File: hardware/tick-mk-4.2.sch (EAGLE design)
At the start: 28 parts, among them IC1 ATMEGA328P, IC2 DS1338, IC3 LM1117, Y1 16MHz

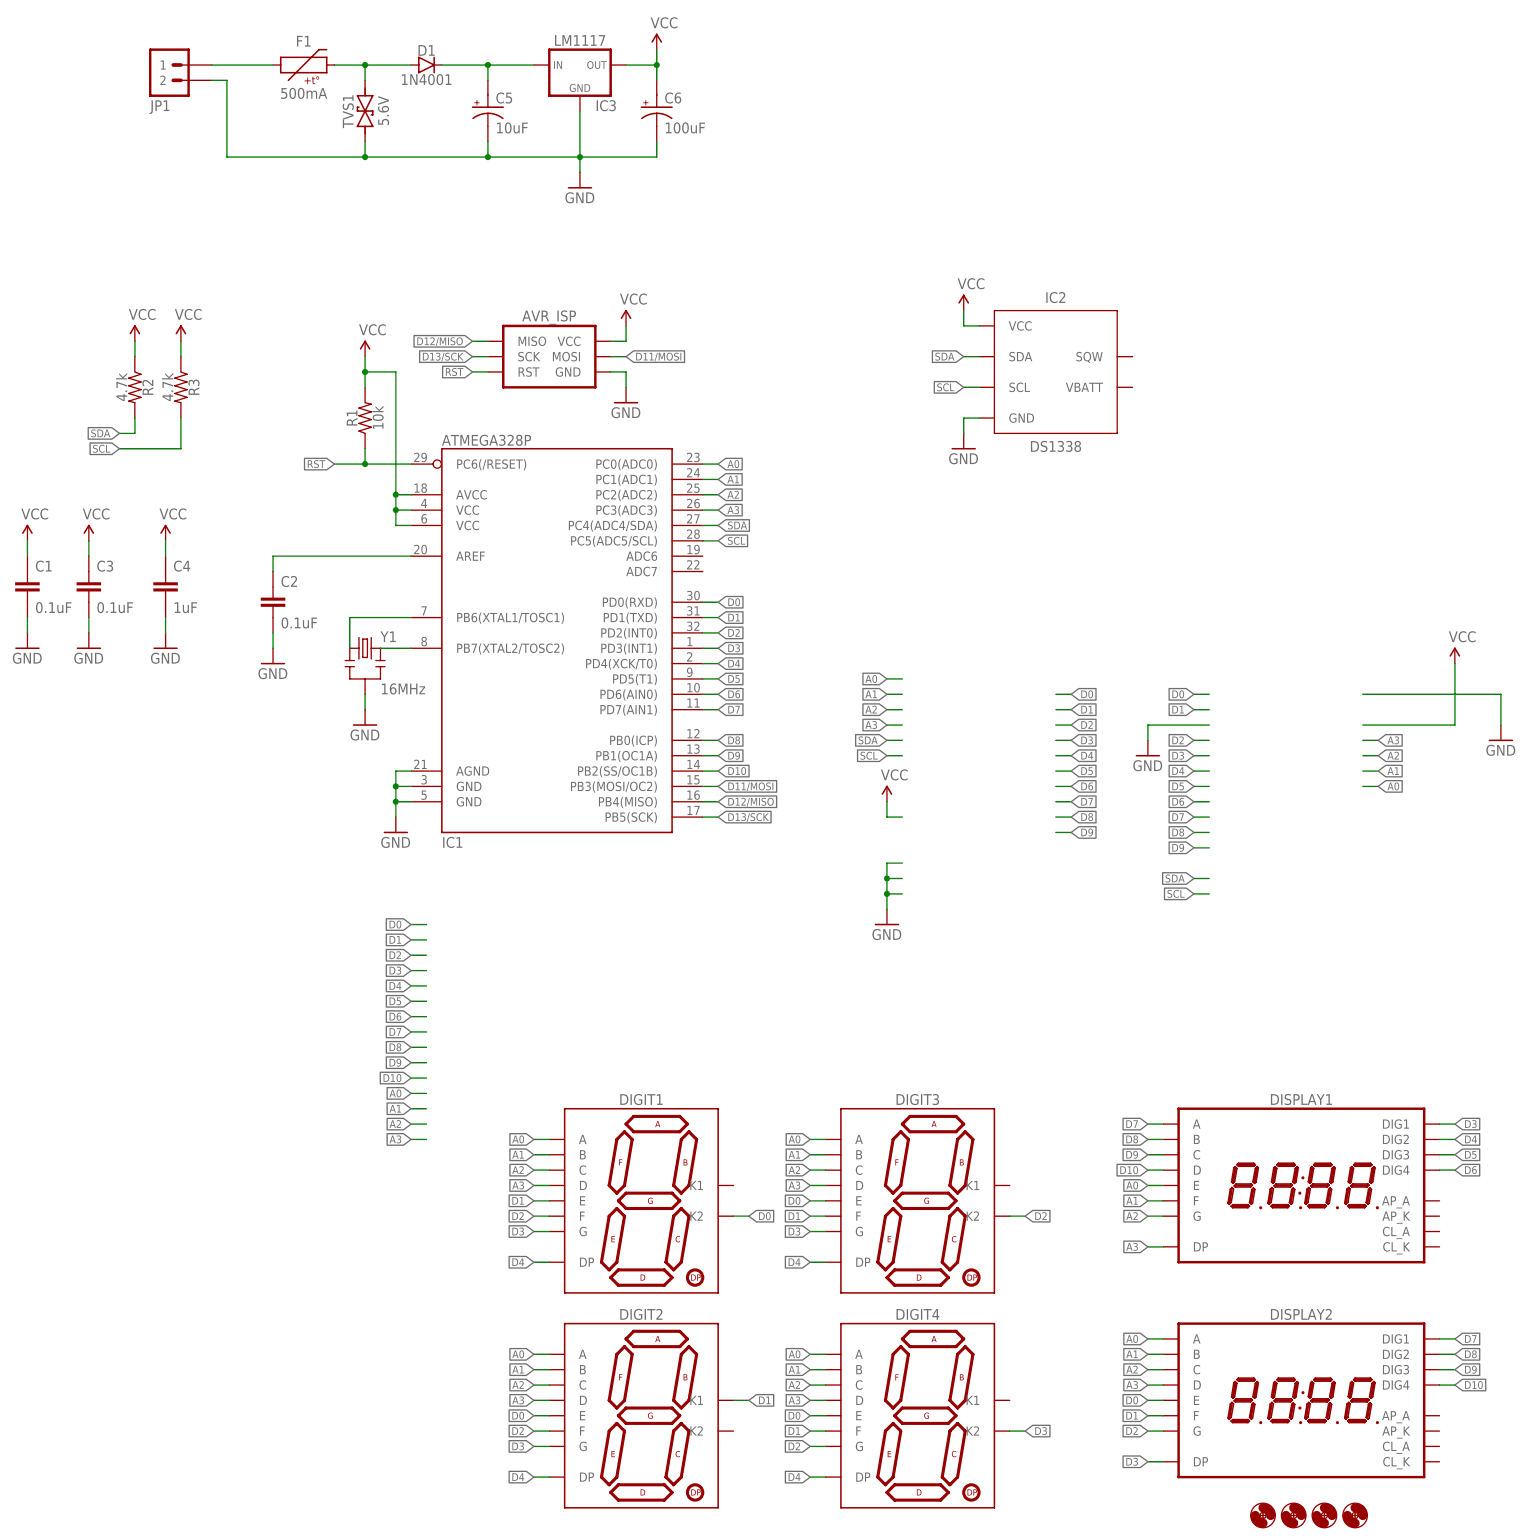
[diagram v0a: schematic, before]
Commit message: swapping most SMD components to PTH ones except for the ICs
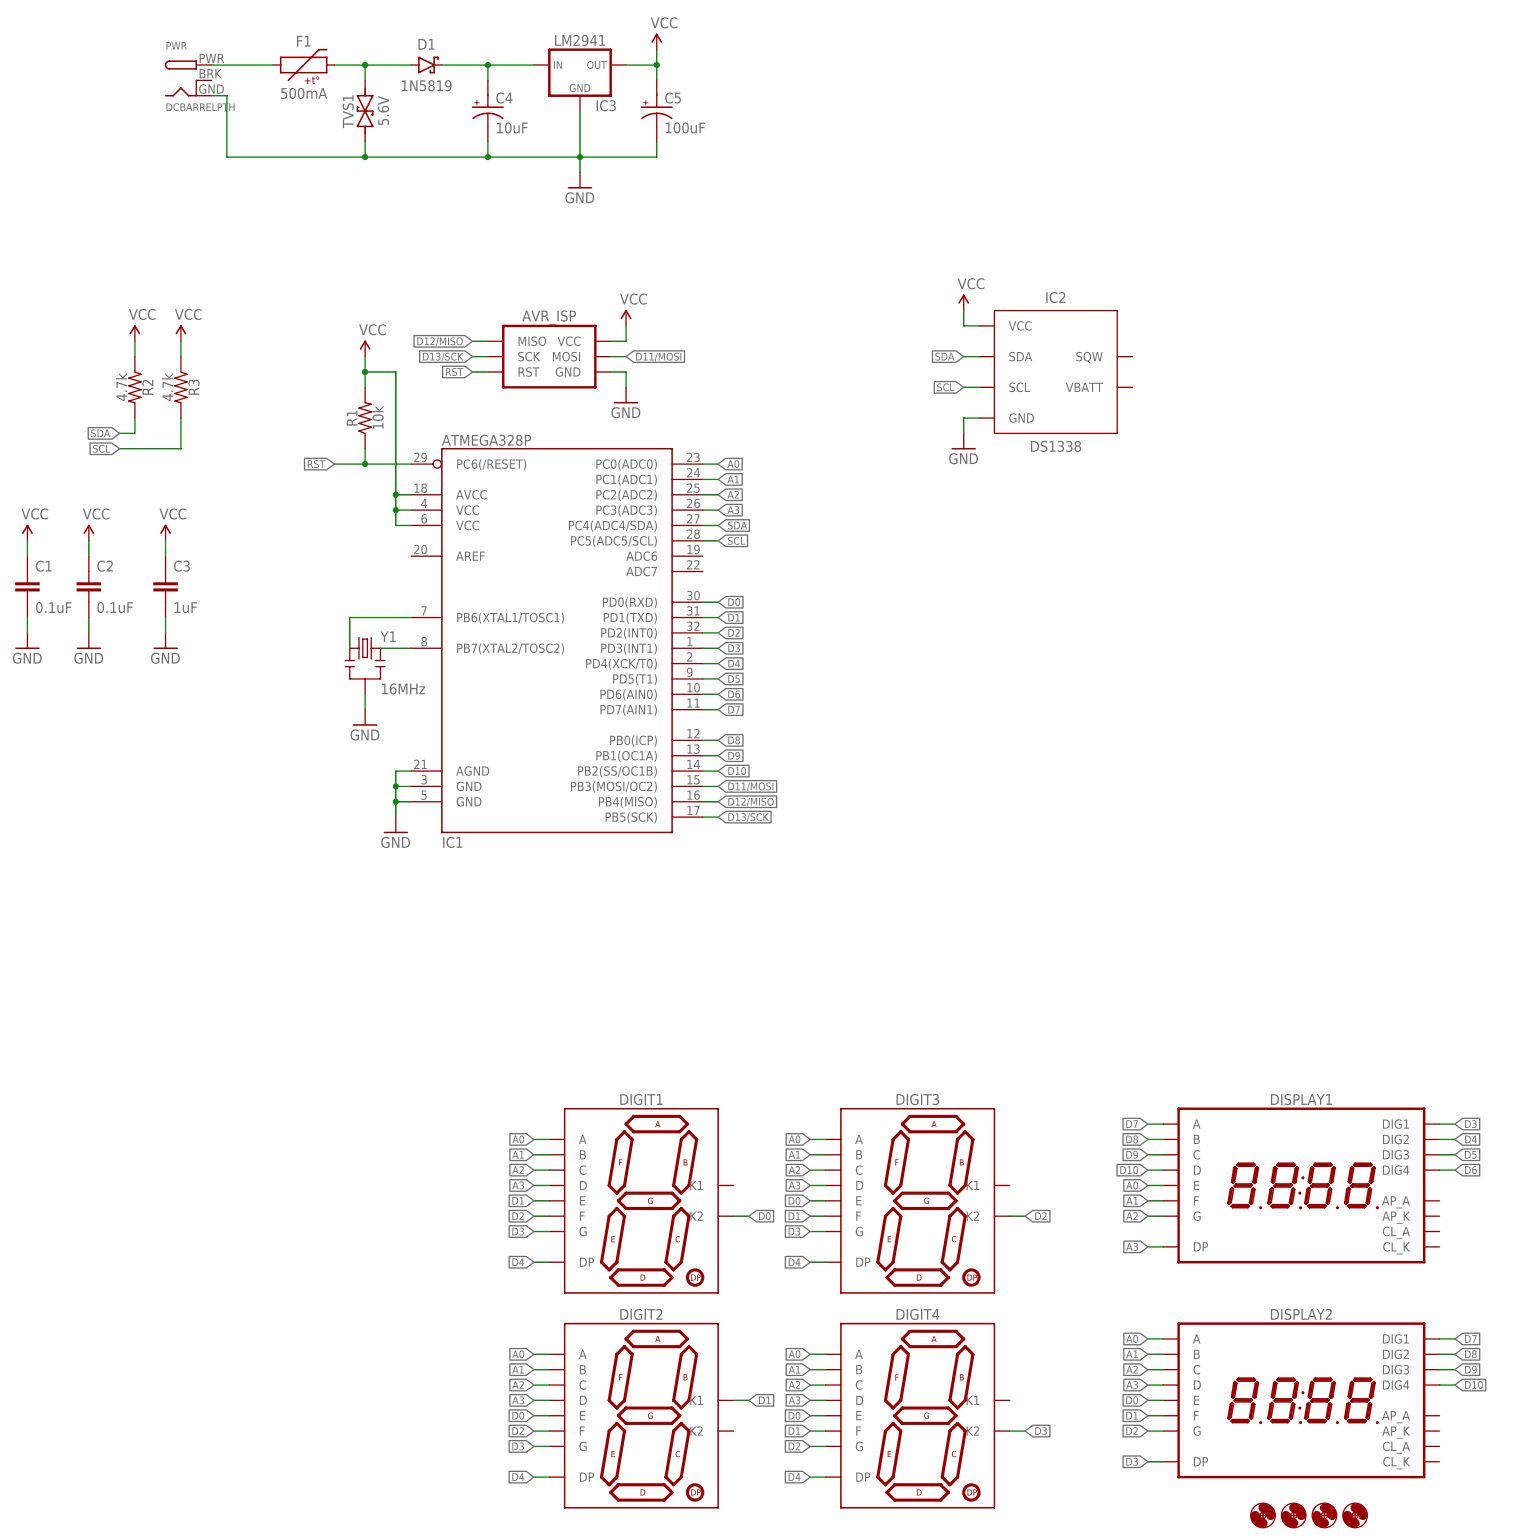
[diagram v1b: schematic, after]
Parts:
- removed C6: 100uF, A_butts:CAPACITOR-POLARIZEDE2.5-6
- removed JP1: M02JST-PTH-VERT, A_butts:M02JST-PTH-VERT
- added PWR: DCBARRELPTH, A_butts:DCBARRELPTH
- C1, C2: device A_butts:CAPACITOR-CERAMICC0805 -> A_butts:CAPACITOR-CERAMIC025-024X044
- C3: value 0.1uF -> 1uF; device A_butts:CAPACITOR-CERAMICC0805 -> A_butts:CAPACITOR-CERAMIC025-024X044
- C4: value 1uF -> 10uF; device A_butts:CAPACITOR-CERAMICC0805 -> A_butts:CAPACITOR-POLARIZEDE2-5
- C5: value 10uF -> 100uF; device A_butts:CAPACITOR-POLARIZEDE2-5 -> A_butts:CAPACITOR-POLARIZEDE2.5-6
- D1: value 1N4001 -> 1N5819; device A_butts:DIODESMA -> A_butts:DIODE-SCHOTTKYPTH-10.16MM
- F1: device A_butts:PTCSMD -> A_butts:PTCPTH-5.08MM
- IC3: value LM1117 -> LM2941; device A_butts:V_REG_78XXSOT-223 -> A_butts:V_REG_78XXTO-92-INLINE
- R1, R2, R3: device A_butts:RESISTORR0805 -> A_butts:RESISTORPTH-AXIAL-6.35MM
- Y1: device A_butts:RESONATORSMD-4.7X4.1X1.2 -> A_butts:RESONATORPTH
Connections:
- removed net N$1: C2.1, IC1.AREF
- net GND: now also C4.-, PWR.GND; no longer C4.2, C6.-, JP1.2
- net N$7: now also PWR.PWR; no longer JP1.1
- net N$8: now also C4.+; no longer C5.+
- net VCC: now also C2.1, C5.+; no longer C4.1, C6.+
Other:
- moved on the sheet: C2, C3, C5

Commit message: layout complete for rev 4.2
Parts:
- added BAT1: 20mm coincell, A_butts:BATTERY20MMSMD-MINE
- DIGIT1, DIGIT2, DIGIT3, DIGIT4: value 7SEG_1DIGPTH-25.4MM -> 7SEG_1DIGPTH-25.4MM-BARE; device A_butts:7SEG_1DIGPTH-25.4MM -> A_butts:7SEG_1DIGPTH-25.4MM-BARE
- IC3: value LM2941 -> L7805; device A_butts:V_REG_78XXTO-92-INLINE -> A_butts:V_REG_78XXTO-220-THERMPAD
- PWR: value DCBARRELPTH -> M02JST-PTH-VERT; device A_butts:DCBARRELPTH -> A_butts:M02JST-PTH-VERT
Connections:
- new net N$1: BAT1.+, IC2.VBATT
- net GND: now also BAT1.-, PWR.1; no longer PWR.GND
- net N$7: now also PWR.2; no longer PWR.PWR
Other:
- moved on the sheet: C4, C5, D1, F1, IC3, TVS1
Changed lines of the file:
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@@
 <layer number="20" name="Dimension" color="15" fill="1" visible="yes" active="no"/>
 <layer number="21" name="tPlace" color="7" fill="1" visible="yes" active="no"/>
-<layer number="22" name="bPlace" color="7" fill="1" visible="yes" active="no"/>
+<layer number="22" name="bPlace" color="6" fill="1" visible="yes" active="no"/>
 <layer number="23" name="tOrigins" color="15" fill="1" visible="yes" active="no"/>
 <layer number="24" name="bOrigins" color="15" fill="1" visible="yes" active="no"/>
@@
 <layer number="45" name="Holes" color="7" fill="1" visible="no" active="no"/>
 <layer number="46" name="Milling" color="3" fill="1" visible="yes" active="no"/>
-<layer number="47" name="Measures" color="7" fill="1" visible="yes" active="no"/>
+<layer number="47" name="Measures" color="5" fill="1" visible="yes" active="no"/>
 <layer number="48" name="Document" color="7" fill="1" visible="yes" active="no"/>
 <layer number="49" name="Reference" color="7" fill="1" visible="yes" active="no"/>
@@
 <part name="H4" library="A_butts" deviceset="HOLE" device="#2" value="HOLE#2"/>
 <part name="DISPLAY2" library="A_butts" deviceset="7SEG_4DIGIT_COLON_APOS" device=""/>
-<part name="DIGIT2" library="A_butts" deviceset="7SEG_1DIG" device="PTH-25.4MM"/>
-<part name="DIGIT1" library="A_butts" deviceset="7SEG_1DIG" device="PTH-25.4MM"/>
-<part name="DIGIT3" library="A_butts" deviceset="7SEG_1DIG" device="PTH-25.4MM"/>
-<part name="DIGIT4" library="A_butts" deviceset="7SEG_1DIG" device="PTH-25.4MM"/>
+<part name="DIGIT2" library="A_butts" deviceset="7SEG_1DIG" device="PTH-25.4MM-BARE" value="7SEG_1DIGPTH-25.4MM-BARE"/>
+<part name="DIGIT1" library="A_butts" deviceset="7SEG_1DIG" device="PTH-25.4MM-BARE" value="7SEG_1DIGPTH-25.4MM-BARE"/>
+<part name="DIGIT3" library="A_butts" deviceset="7SEG_1DIG" device="PTH-25.4MM-BARE" value="7SEG_1DIGPTH-25.4MM-BARE"/>
+<part name="DIGIT4" library="A_butts" deviceset="7SEG_1DIG" device="PTH-25.4MM-BARE" value="7SEG_1DIGPTH-25.4MM-BARE"/>
 <part name="DISPLAY1" library="A_butts" deviceset="7SEG_4DIGIT_COLON_APOS" device=""/>
 <part name="IC1" library="A_butts" deviceset="ATMEGA328_SMT" device="" value="ATMEGA328P"/>
@@
 <part name="C4" library="A_butts" deviceset="CAPACITOR-POLARIZED" device="E2-5" value="10uF"/>
 <part name="C5" library="A_butts" deviceset="CAPACITOR-POLARIZED" device="E2.5-6" value="100uF"/>
-<part name="IC3" library="A_butts" deviceset="V_REG_78XX" device="TO-92-INLINE" value="LM2941"/>
+<part name="IC3" library="A_butts" deviceset="V_REG_78XX" device="TO-220-THERMPAD" value="L7805"/>
 <part name="D1" library="A_butts" deviceset="DIODE-SCHOTTKY" device="PTH-10.16MM" value="1N5819"/>
-<part name="PWR" library="A_butts" deviceset="DCBARREL" device="PTH"/>
+<part name="PWR" library="A_butts" deviceset="M02" device="JST-PTH-VERT"/>
+<part name="BAT1" library="A_butts" deviceset="BATTERY" device="20MMSMD-MINE" value="20mm coincell"/>
+<part name="GND1" library="A_butts" deviceset="GND" device=""/>
 </parts>
 <sheets>
@@
 <instance part="R3" gate="G$1" x="2.54" y="198.12" rot="R270"/>
 <instance part="SUPPLY10" gate="G$1" x="2.54" y="205.74"/>
-<instance part="SUPPLY15" gate="G$1" x="81.28" y="254"/>
-<instance part="GND12" gate="1" x="68.58" y="231.14"/>
-<instance part="TVS1" gate="G$1" x="33.02" y="243.84" rot="R90"/>
-<instance part="F1" gate="G$1" x="22.86" y="251.46"/>
-<instance part="C4" gate="G$1" x="53.34" y="243.84"/>
-<instance part="C5" gate="G$1" x="81.28" y="243.84"/>
-<instance part="IC3" gate="G$1" x="68.58" y="251.46"/>
-<instance part="D1" gate="G$1" x="43.18" y="251.46"/>
-<instance part="PWR" gate="G$1" x="5.08" y="248.92"/>
+<instance part="SUPPLY15" gate="G$1" x="76.2" y="254"/>
+<instance part="GND12" gate="1" x="63.5" y="231.14"/>
+<instance part="TVS1" gate="G$1" x="27.94" y="243.84" rot="R90"/>
+<instance part="F1" gate="G$1" x="17.78" y="251.46"/>
+<instance part="C4" gate="G$1" x="48.26" y="243.84"/>
+<instance part="C5" gate="G$1" x="76.2" y="243.84"/>
+<instance part="IC3" gate="G$1" x="63.5" y="251.46"/>
+<instance part="D1" gate="G$1" x="38.1" y="251.46"/>
+<instance part="PWR" gate="G$1" x="-5.08" y="246.38"/>
+<instance part="BAT1" gate="G$1" x="167.64" y="198.12"/>
+<instance part="GND1" gate="1" x="175.26" y="193.04"/>
 </instances>
 <busses>
@@
 </segment>
 <segment>
-<wire x1="76.2" y1="251.46" x2="81.28" y2="251.46" width="0.1524" layer="91"/>
+<wire x1="71.12" y1="251.46" x2="76.2" y2="251.46" width="0.1524" layer="91"/>
 <pinref part="SUPPLY15" gate="G$1" pin="VCC"/>
-<wire x1="81.28" y1="251.46" x2="81.28" y2="254" width="0.1524" layer="91"/>
-<wire x1="81.28" y1="248.92" x2="81.28" y2="251.46" width="0.1524" layer="91"/>
-<junction x="81.28" y="251.46"/>
+<wire x1="76.2" y1="251.46" x2="76.2" y2="254" width="0.1524" layer="91"/>
+<wire x1="76.2" y1="248.92" x2="76.2" y2="251.46" width="0.1524" layer="91"/>
+<junction x="76.2" y="251.46"/>
 <pinref part="C5" gate="G$1" pin="+"/>
 <pinref part="IC3" gate="G$1" pin="OUT"/>
@@
 </segment>
 <segment>
-<wire x1="53.34" y1="238.76" x2="53.34" y2="236.22" width="0.1524" layer="91"/>
-<wire x1="81.28" y1="238.76" x2="81.28" y2="236.22" width="0.1524" layer="91"/>
-<wire x1="81.28" y1="236.22" x2="68.58" y2="236.22" width="0.1524" layer="91"/>
+<wire x1="48.26" y1="238.76" x2="48.26" y2="236.22" width="0.1524" layer="91"/>
+<wire x1="76.2" y1="238.76" x2="76.2" y2="236.22" width="0.1524" layer="91"/>
+<wire x1="76.2" y1="236.22" x2="63.5" y2="236.22" width="0.1524" layer="91"/>
 <pinref part="GND12" gate="1" pin="GND"/>
-<wire x1="68.58" y1="236.22" x2="53.34" y2="236.22" width="0.1524" layer="91"/>
-<wire x1="68.58" y1="233.68" x2="68.58" y2="236.22" width="0.1524" layer="91"/>
-<junction x="68.58" y="236.22"/>
-<wire x1="10.16" y1="246.38" x2="10.16" y2="236.22" width="0.1524" layer="91"/>
-<wire x1="10.16" y1="236.22" x2="33.02" y2="236.22" width="0.1524" layer="91"/>
-<junction x="53.34" y="236.22"/>
+<wire x1="63.5" y1="236.22" x2="48.26" y2="236.22" width="0.1524" layer="91"/>
+<wire x1="63.5" y1="233.68" x2="63.5" y2="236.22" width="0.1524" layer="91"/>
+<junction x="63.5" y="236.22"/>
+<junction x="48.26" y="236.22"/>
 <pinref part="TVS1" gate="G$1" pin="1"/>
-<wire x1="33.02" y1="236.22" x2="53.34" y2="236.22" width="0.1524" layer="91"/>
-<wire x1="33.02" y1="238.76" x2="33.02" y2="236.22" width="0.1524" layer="91"/>
-<junction x="33.02" y="236.22"/>
-<wire x1="10.16" y1="246.38" x2="7.62" y2="246.38" width="0.1524" layer="91"/>
-<wire x1="68.58" y1="243.84" x2="68.58" y2="236.22" width="0.1524" layer="91"/>
+<wire x1="7.62" y1="236.22" x2="27.94" y2="236.22" width="0.1524" layer="91"/>
+<wire x1="27.94" y1="236.22" x2="48.26" y2="236.22" width="0.1524" layer="91"/>
+<wire x1="27.94" y1="238.76" x2="27.94" y2="236.22" width="0.1524" layer="91"/>
+<junction x="27.94" y="236.22"/>
+<wire x1="63.5" y1="243.84" x2="63.5" y2="236.22" width="0.1524" layer="91"/>
 <pinref part="C4" gate="G$1" pin="-"/>
 <pinref part="C5" gate="G$1" pin="-"/>
 <pinref part="IC3" gate="G$1" pin="GND"/>
-<pinref part="PWR" gate="G$1" pin="GND"/>
+<pinref part="PWR" gate="G$1" pin="1"/>
+<wire x1="5.08" y1="248.92" x2="7.62" y2="248.92" width="0.1524" layer="91"/>
+<wire x1="7.62" y1="248.92" x2="7.62" y2="236.22" width="0.1524" layer="91"/>
+</segment>
+<segment>
+<pinref part="BAT1" gate="G$1" pin="-"/>
+<wire x1="172.72" y1="198.12" x2="175.26" y2="198.12" width="0.1524" layer="91"/>
+<pinref part="GND1" gate="1" pin="GND"/>
+<wire x1="175.26" y1="198.12" x2="175.26" y2="195.58" width="0.1524" layer="91"/>
 </segment>
 </net>
@@
 <segment>
 <pinref part="F1" gate="G$1" pin="1"/>
-<wire x1="17.78" y1="251.46" x2="7.62" y2="251.46" width="0.1524" layer="91"/>
-<pinref part="PWR" gate="G$1" pin="PWR"/>
+<pinref part="PWR" gate="G$1" pin="2"/>
+<wire x1="5.08" y1="251.46" x2="12.7" y2="251.46" width="0.1524" layer="91"/>
 </segment>
 </net>
 <net name="N$8" class="0">
 <segment>
-<wire x1="53.34" y1="248.92" x2="53.34" y2="251.46" width="0.1524" layer="91"/>
-<wire x1="53.34" y1="251.46" x2="60.96" y2="251.46" width="0.1524" layer="91"/>
+<wire x1="48.26" y1="248.92" x2="48.26" y2="251.46" width="0.1524" layer="91"/>
+<wire x1="48.26" y1="251.46" x2="55.88" y2="251.46" width="0.1524" layer="91"/>
 <pinref part="C4" gate="G$1" pin="+"/>
 <pinref part="IC3" gate="G$1" pin="IN"/>
 <pinref part="D1" gate="G$1" pin="C"/>
-<wire x1="45.72" y1="251.46" x2="53.34" y2="251.46" width="0.1524" layer="91"/>
-<junction x="53.34" y="251.46"/>
+<wire x1="40.64" y1="251.46" x2="48.26" y2="251.46" width="0.1524" layer="91"/>
+<junction x="48.26" y="251.46"/>
 </segment>
 </net>
@@
 <segment>
 <pinref part="TVS1" gate="G$1" pin="2"/>
-<wire x1="33.02" y1="251.46" x2="33.02" y2="248.92" width="0.1524" layer="91"/>
+<wire x1="27.94" y1="251.46" x2="27.94" y2="248.92" width="0.1524" layer="91"/>
 <pinref part="F1" gate="G$1" pin="2"/>
-<wire x1="27.94" y1="251.46" x2="33.02" y2="251.46" width="0.1524" layer="91"/>
+<wire x1="22.86" y1="251.46" x2="27.94" y2="251.46" width="0.1524" layer="91"/>
 <pinref part="D1" gate="G$1" pin="A"/>
-<wire x1="33.02" y1="251.46" x2="40.64" y2="251.46" width="0.1524" layer="91"/>
-<junction x="33.02" y="251.46"/>
-</segment>
-</net>
+<wire x1="27.94" y1="251.46" x2="35.56" y2="251.46" width="0.1524" layer="91"/>
+<junction x="27.94" y="251.46"/>
+</segment>
+</net>
+<net name="N$1" class="0">
+<segment>
+<pinref part="IC2" gate="G$1" pin="VBATT"/>
+<pinref part="BAT1" gate="G$1" pin="+"/>
+<wire x1="162.56" y1="198.12" x2="160.02" y2="198.12" width="0.1524" layer="91"/>
+</segment>
+</net>
